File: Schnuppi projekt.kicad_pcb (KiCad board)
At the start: 2 copper layers, 21 parts, among them Q1 BC817, Q2 BC817, SW1 SW_Push, SW2 SW_Push, SW3 SW_Push, SW4 SW_Push, SW5 SW_Push, SW6 SW_Push, U13 ESP32-WROOM-32E, U2 TPS62065DSGR, U5 WE-TVS-82400102, U6 CH340C

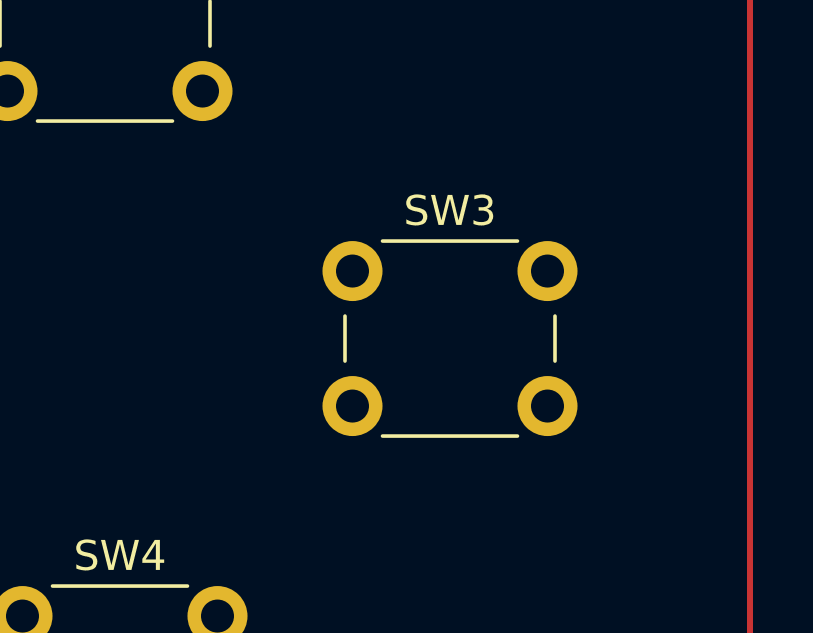
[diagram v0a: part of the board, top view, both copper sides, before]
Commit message: Button changed
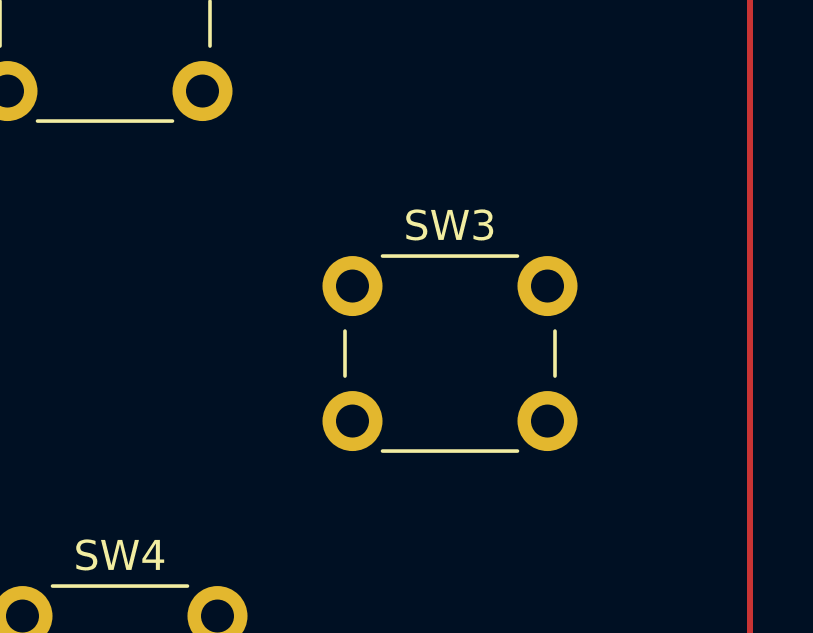
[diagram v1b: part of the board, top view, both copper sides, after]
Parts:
- moved SW3 0.50 mm to (86.8, 56.8)
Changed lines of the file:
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@@
 	(footprint "Button_Switch_THT:SW_PUSH_6mm_H4.3mm"
 		(layer "F.Cu")
-		(at 86.75 56.25)
+		(at 86.75 56.75)
 		(descr "tactile push button, 6x6mm e.g. PHAP33xx series, height=4.3mm")
 		(tags "tact sw push 6mm")
